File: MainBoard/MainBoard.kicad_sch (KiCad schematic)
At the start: 42 parts, among them J1 1761681-3, Q1 BC557, U1 LM393, U2 TL074

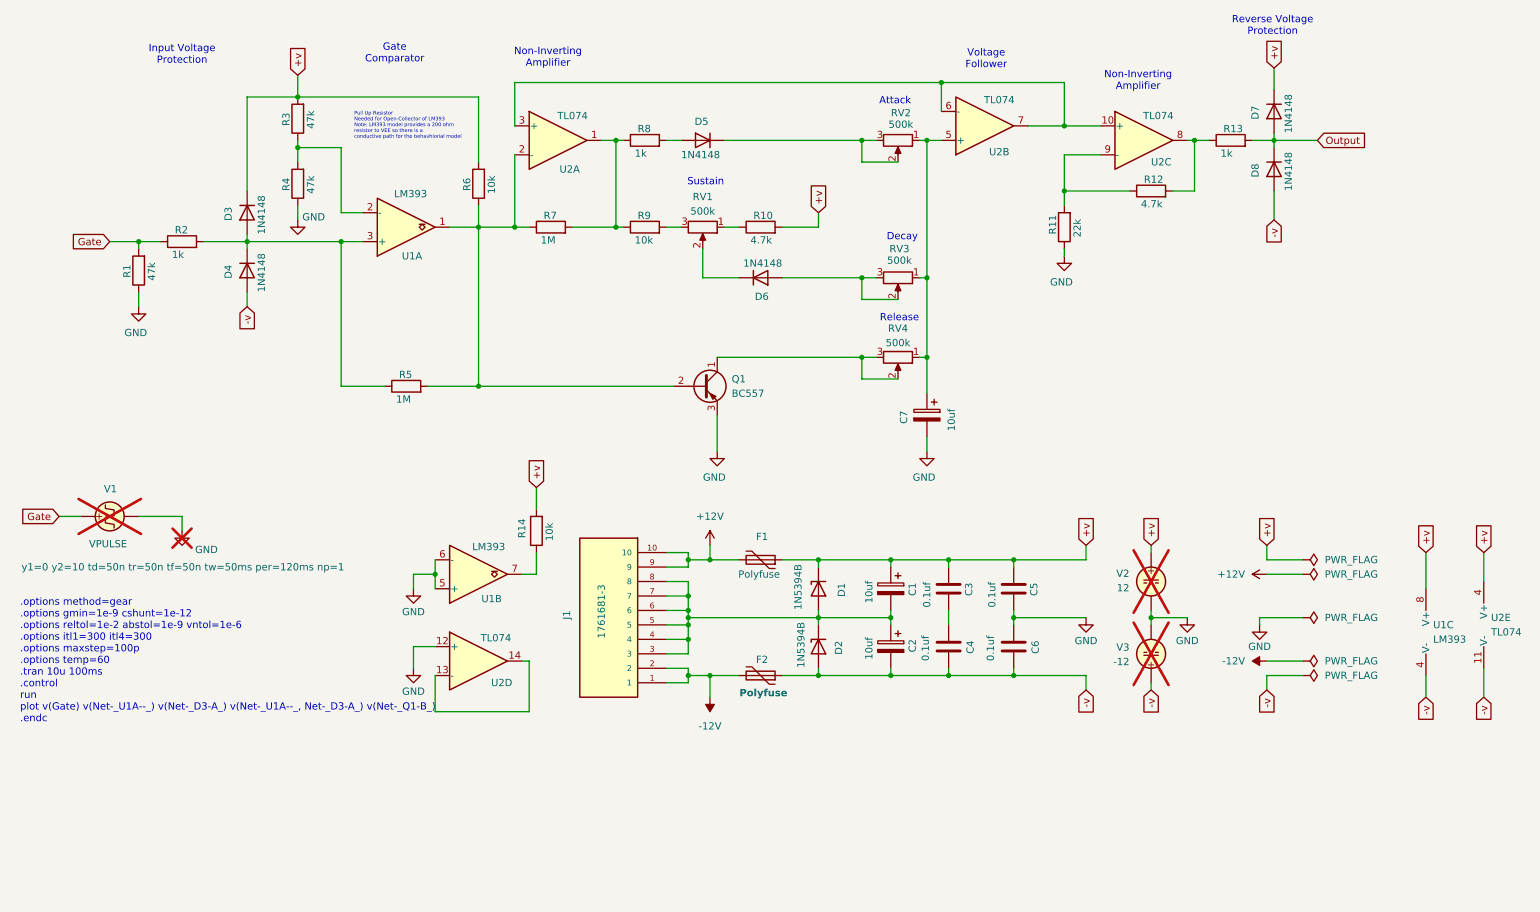
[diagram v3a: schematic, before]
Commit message: lm393 model w/ transistor
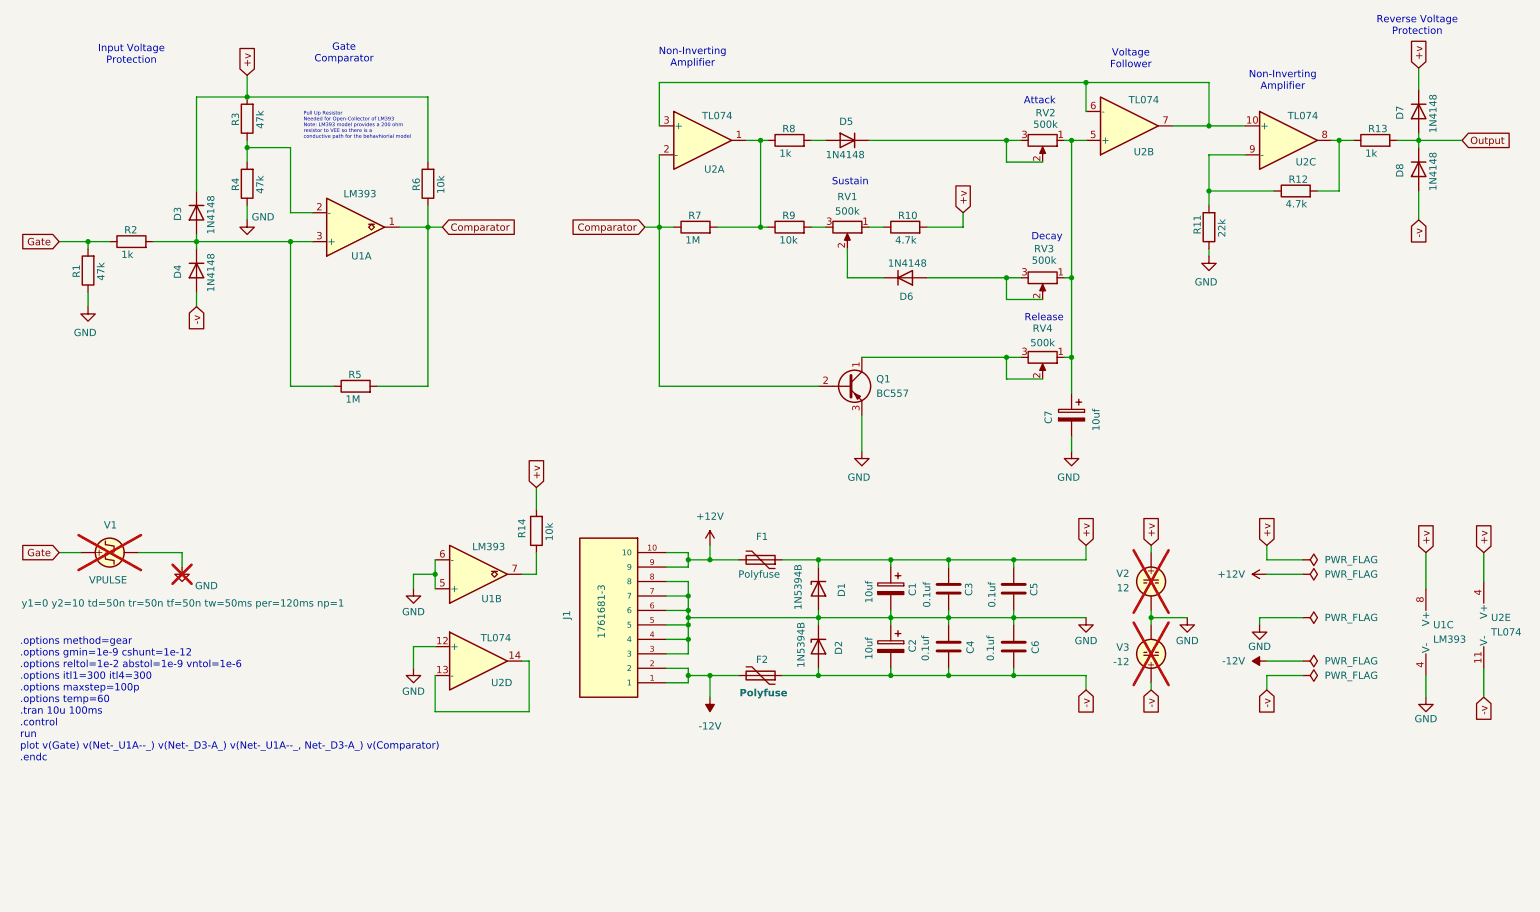
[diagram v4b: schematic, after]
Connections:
- net -v: no longer U1.4 (V-)
- net GND: now also C1.2, C2.1, C3.2, C4.1, D1.2 (A), D2.1 (K), J1.3, J1.4, J1.5, J1.6, J1.7, J1.8, U1.4 (V-)
- net Comparator: now reaches Q1.2 (B), R5.2, R6.1, R7.1, U1.1, U2.2 (-)
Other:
- note added: ".options method=gear .options gmin=1e-9 cshunt=1e-12 .options reltol=1e-2 abstol=1e-9 vntol=1e-6 .options itl1=300 itl4=300 .options maxstep=100p .options temp=60 .tran 10u 100ms .control run plot v(Gate) v(Net-_U1A--_) v(Net-_D3-A_) v(Net-_U1A--_, Net-_D3-A_) v(Comparator) .endc"
- note removed: ".options method=gear .options gmin=1e-9 cshunt=1e-12 .options reltol=1e-2 abstol=1e-9 vntol=1e-6 .options itl1=300 itl4=300 .options maxstep=100p .options temp=60 .tran 10u 100ms .control run plot v(Gate) v(Net-_U1A--_) v(Net-_D3-A_) v(Net-_U1A--_, Net-_D3-A_) v(Net-_Q1-B_) .endc"
- moved on the sheet: C7, D3, D4, D5, D6, D7, D8, Q1, R1, R10, R11, R12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
